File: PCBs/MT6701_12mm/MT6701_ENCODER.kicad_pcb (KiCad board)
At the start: 2 copper layers, 16.2 x 16.1 mm, 6 parts, among them J5 Conn_01x05, U1 MT6701CT

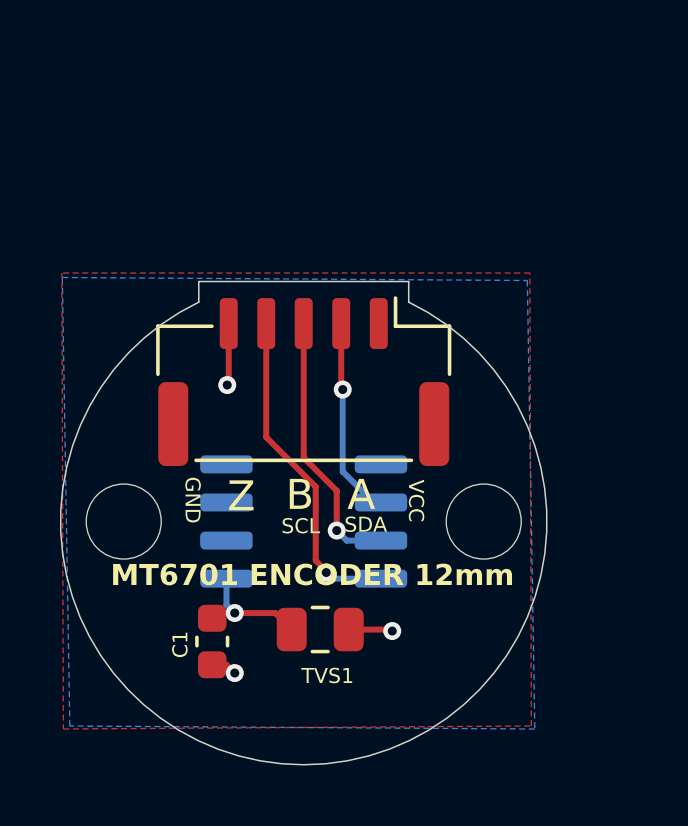
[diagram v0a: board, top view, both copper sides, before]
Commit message: version 2 encoder board
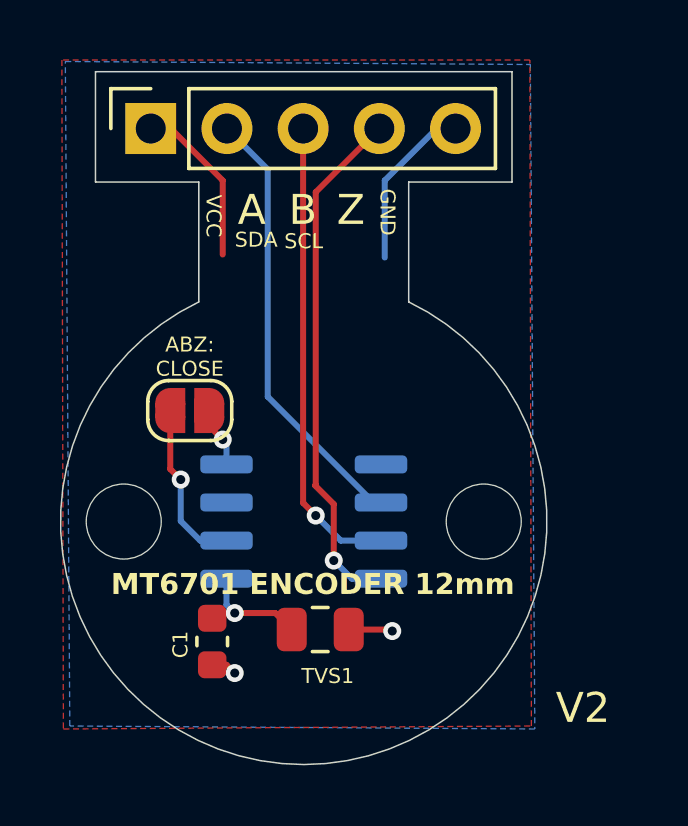
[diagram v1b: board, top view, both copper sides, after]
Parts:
- added JP1: SolderJumper_2_Open, Jumper:SolderJumper-2_P1.3mm_Open_RoundedPad1.0x1.5mm, F.Cu at (96.2, 96.3)
- J5: footprint Connector_JST:JST_GH_BM05B-GHS-TBT_1x05-1MP_P1.25mm_Vertical -> Connector_PinSocket_2.54mm:PinSocket_1x05_P2.54mm_Vertical
- moved J5 9.87 mm to (94.9, 86.9), turned to 90 degrees
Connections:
- U1 pad 2: unconnected-(U1-MODE-Pad2) -> Net-(JP1-A)
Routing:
- net ENC_A: track 7.08 -> 14.7 mm, vias 1 -> 0
- net ENC_Z: track 11.4 -> 17.5 mm
- net ENC_B: track 9.53 -> 15.6 mm
- net Net-(JP1-A): track 0.00 -> 5.62 mm, vias 0 -> 1
- net Vcc: track 4.21 -> 9.79 mm
- net GND: track 4.76 -> 10.0 mm
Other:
- board size 16.2 x 16.1 mm -> 16.2 x 23.1 mm
- board text added: "ABZ: CLOSE"
- board text added: "V2"
